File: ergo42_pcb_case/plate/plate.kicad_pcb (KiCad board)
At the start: 2 copper layers, 138.4 x 81.3 mm, 6 parts

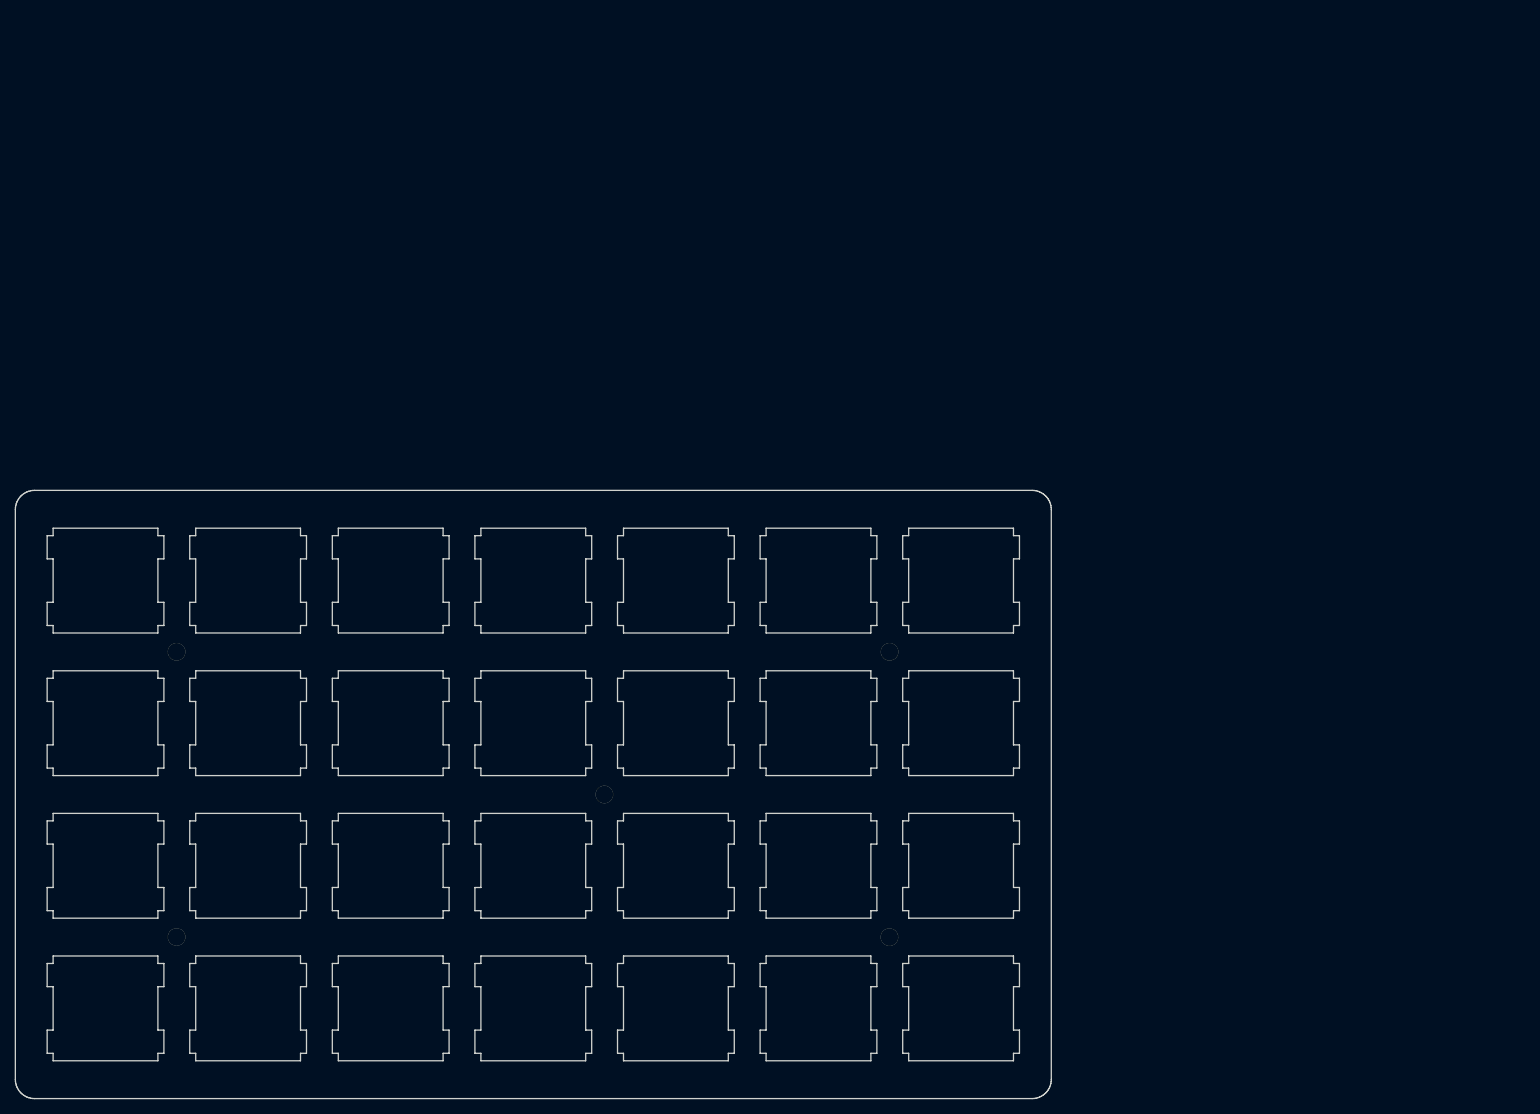
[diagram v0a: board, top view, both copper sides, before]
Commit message: FreeCAD to KiCAD approach
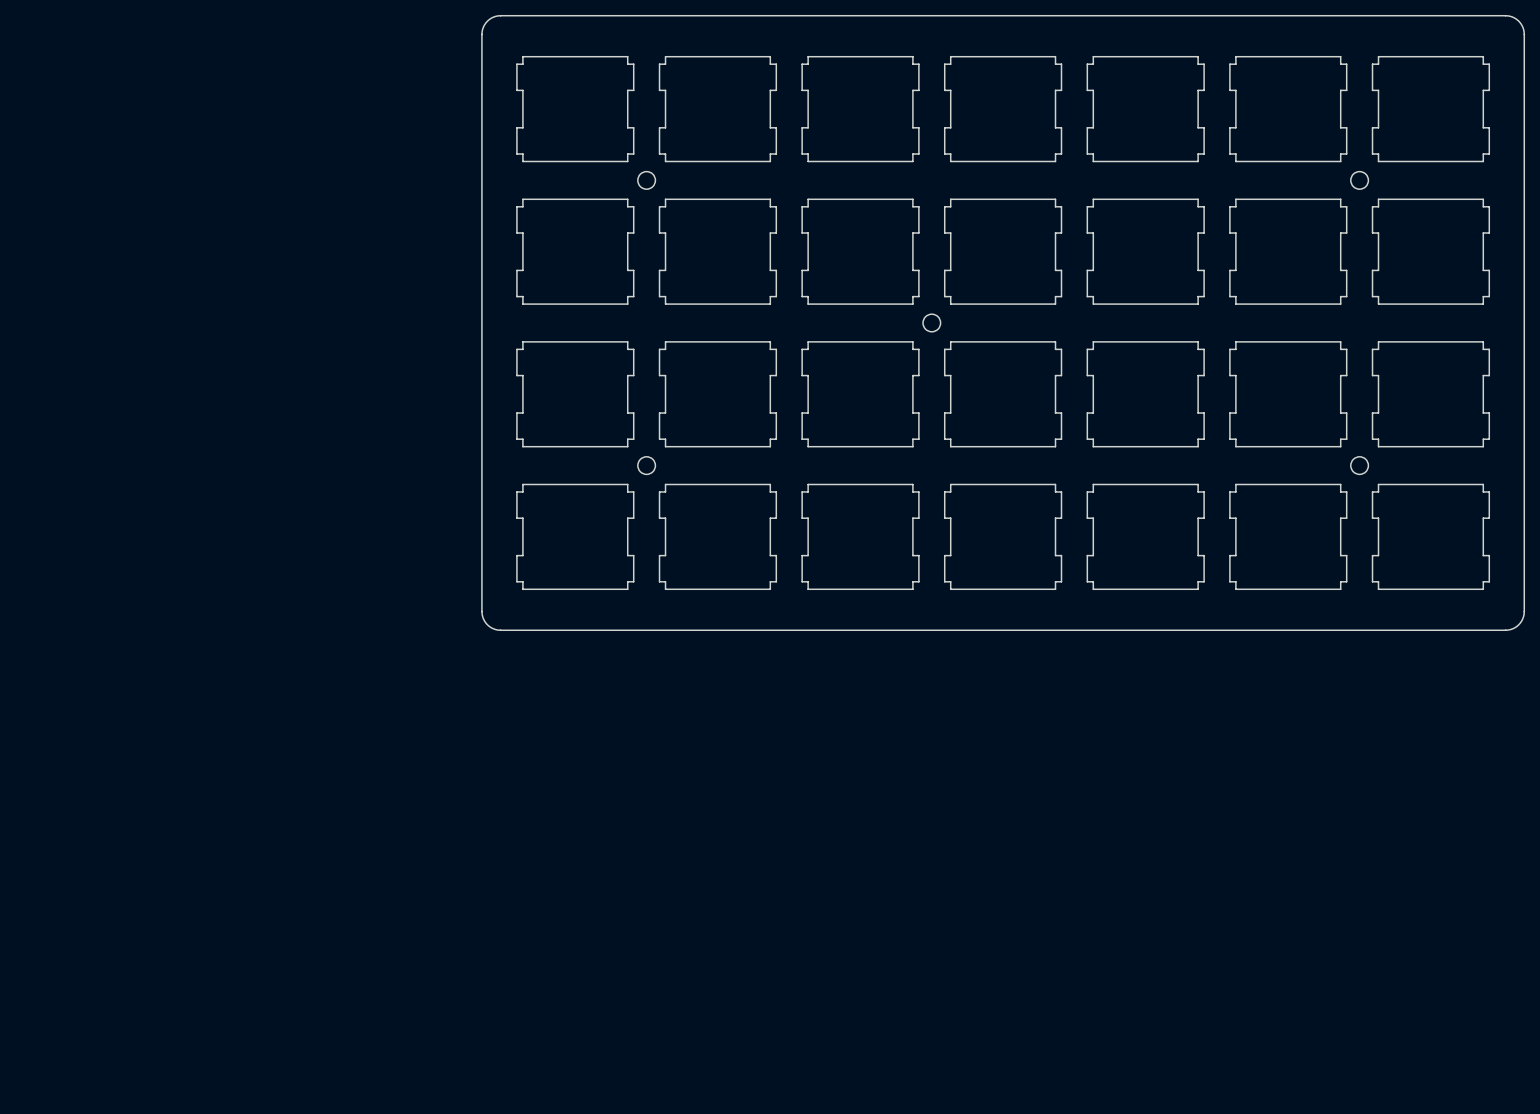
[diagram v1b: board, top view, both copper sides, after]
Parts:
- removed ? (x5): , Wire_Pads:SolderWirePad_single_0-8mmDrill
- removed G***: LOGO, LOGO
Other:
- board size 138.4 x 81.3 mm -> 139.2 x 82.1 mm
- net class Default: via_dia 0.6 -> 0.8
- rule pad_to_mask_clearance: 0.2 -> 0.051

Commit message: DXF -> KiCad -> plots
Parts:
- added REF**: MountingHole_2.2mm_M2_Pad, MountingHole_2.2mm_M2_Pad, F.Cu at (104.8, -47.6)
- added REF**: MountingHole_2.2mm_M2_Pad, MountingHole_2.2mm_M2_Pad, F.Cu at (104.8, -9.53)
- added REF**: MountingHole_2.2mm_M2_Pad, MountingHole_2.2mm_M2_Pad, F.Cu at (47.6, -28.6)
- added REF**: MountingHole_2.2mm_M2_Pad, MountingHole_2.2mm_M2_Pad, F.Cu at (9.53, -9.53)
- added REF**: MountingHole_2.2mm_M2_Pad, MountingHole_2.2mm_M2_Pad, F.Cu at (9.53, -47.6)
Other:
- outline, holes or cut-outs redrawn

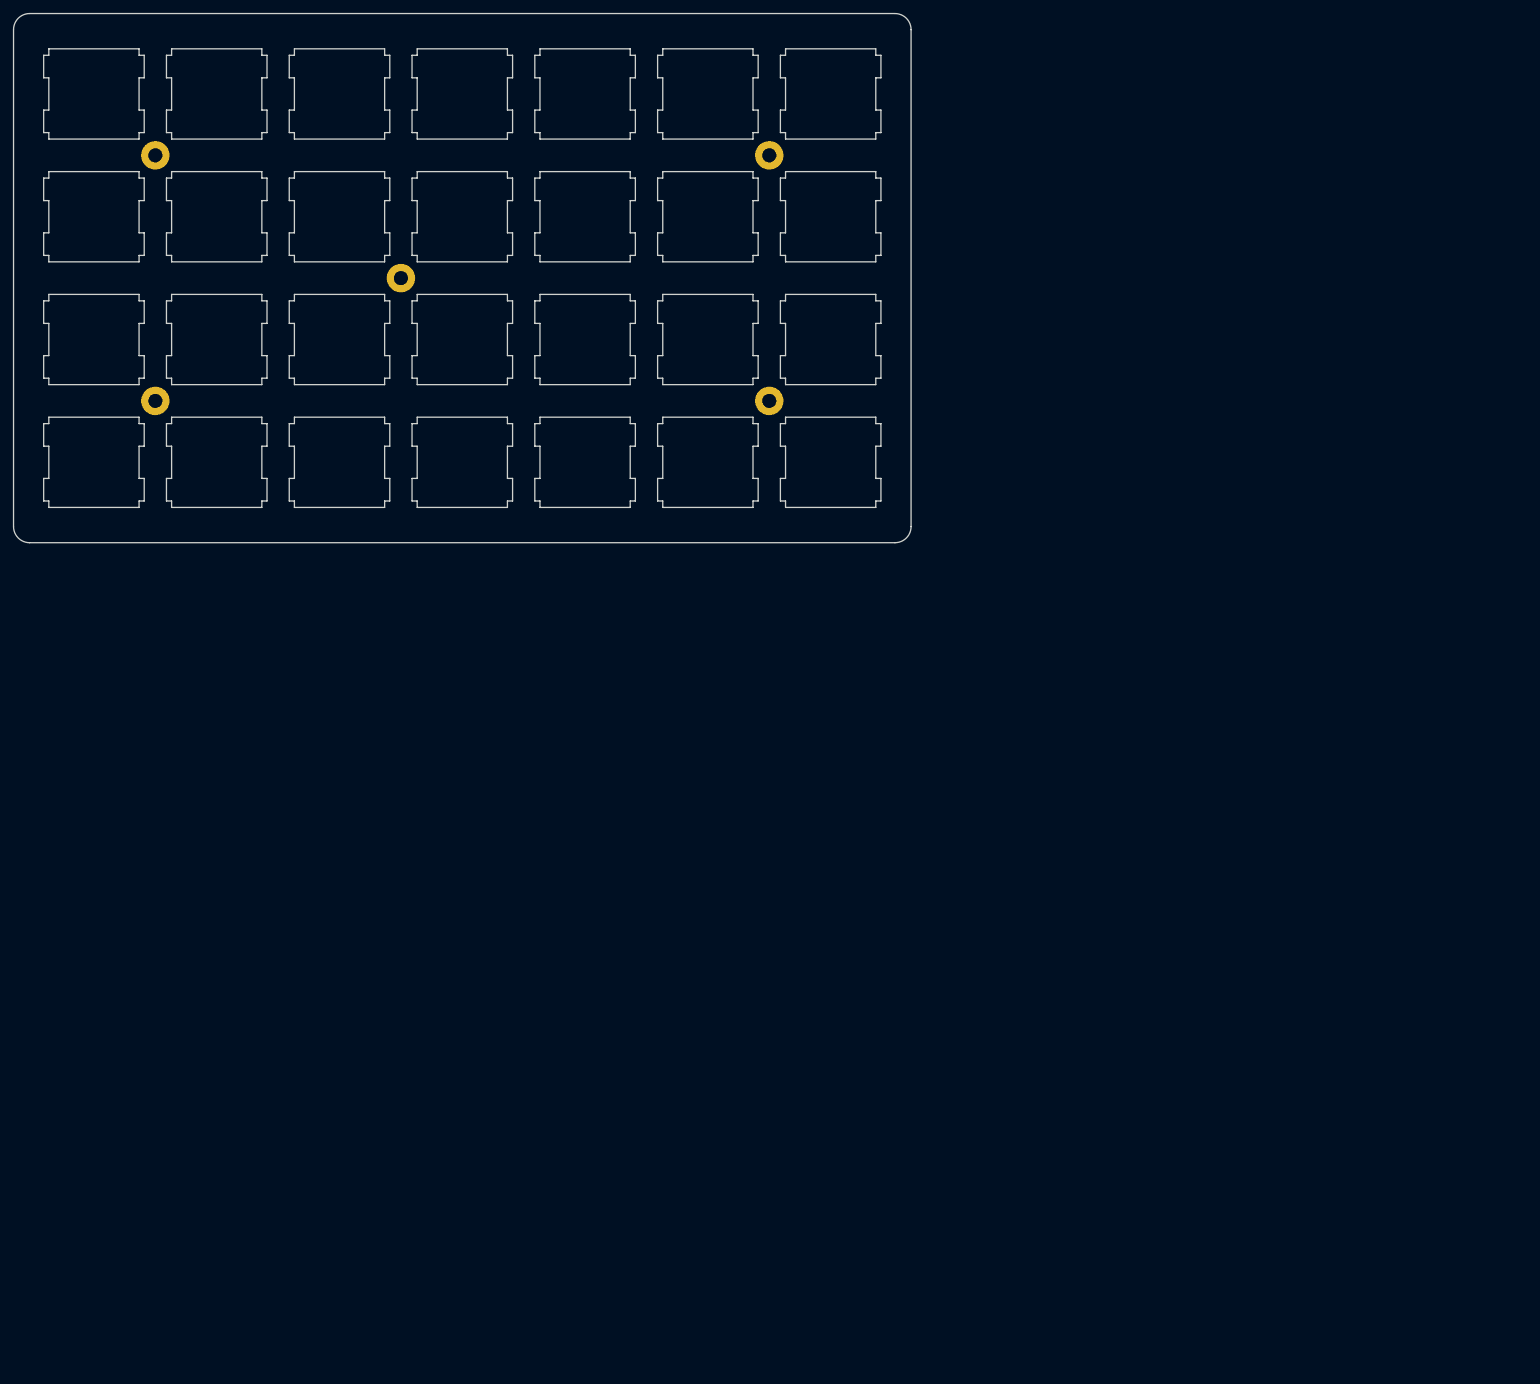
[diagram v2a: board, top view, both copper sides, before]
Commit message: Reimport DXFs into middle of the page
PDF plotter has hard times with anything outside A4 page...
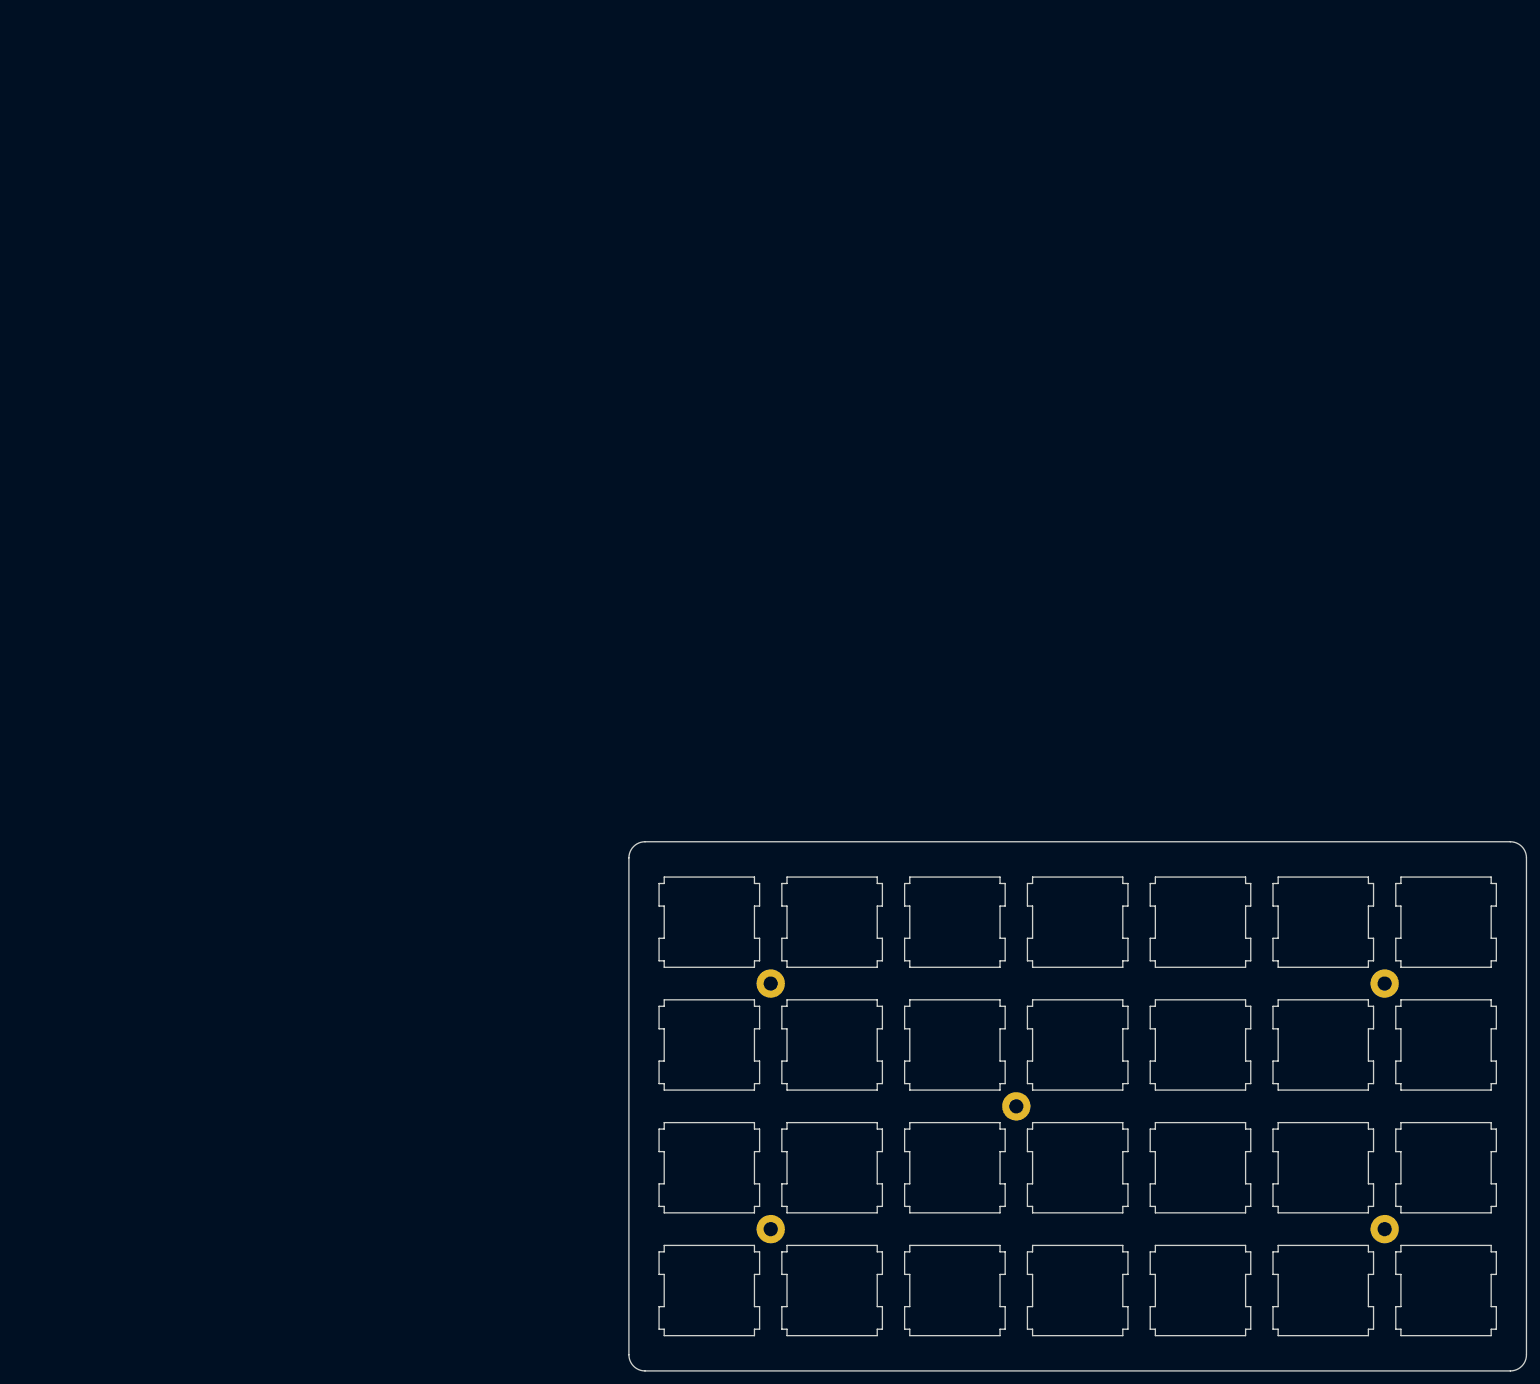
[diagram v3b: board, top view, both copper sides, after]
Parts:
- removed the REF** at (104.8, -47.6)
- removed the REF** at (104.8, -9.53)
- removed the REF** at (47.6, -28.6)
- removed the REF** at (9.53, -9.53)
- removed the REF** at (9.53, -47.6)
- added REF**: MountingHole_2.2mm_M2_Pad, MountingHole_2.2mm_M2_Pad, F.Cu at (200.2, 80.9)
- added REF**: MountingHole_2.2mm_M2_Pad, MountingHole_2.2mm_M2_Pad, F.Cu at (200.2, 119.0)
- added REF**: MountingHole_2.2mm_M2_Pad, MountingHole_2.2mm_M2_Pad, F.Cu at (143.1, 99.9)
- added REF**: MountingHole_2.2mm_M2_Pad, MountingHole_2.2mm_M2_Pad, F.Cu at (105.0, 119.0)
- added REF**: MountingHole_2.2mm_M2_Pad, MountingHole_2.2mm_M2_Pad, F.Cu at (105.0, 80.9)
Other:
- board size 139.2 x 82.1 mm -> 139.3 x 82.1 mm
